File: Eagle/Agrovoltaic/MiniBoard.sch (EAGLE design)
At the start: 56 parts, among them J1 WAGO-03BE, J2 WAGO-03BE, J3 WAGO-03BE, K1 SRD-05VDC-SL-C, K3 SRD-05VDC-SL-C, Q1 BC338, Q2 BC338

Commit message: EDIT:Mengedit Board
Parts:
- removed CA3: 100n, rcl:CPOL-EUE3.5-8
- removed MC1: DEVKIT_V1_ESP32-WROOM-32, DEVKIT_V1_ESP32-WROOM-32:DEVKIT_V1_ESP32-WROOM-32
- added ANALOG, DIGITAL-IN, DIGITAL-OUT: (no value), con-wago-500:W237-102
- added CA4: 100n, rcl:CPOL-EUE3.5-8
- added U$1: CP8-ADJ, userlib:CP8-ADJ
- added U1: ESP32-DEVKIT-V1, ESP32-DEVKIT-V1:ESP32-DEVKIT-V1
- added UART2: 332-02, con-garry:332-02
- R12, R14: value 3K -> 2K
- R25, R26: value 3K -> 180
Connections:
- removed net IO16: MC1.IO16
- removed net IO17: MC1.IO17
- removed net IO4: MC1.IO4
- removed net N$10: IOESP.4
- removed net N$11: IOESP.5
- removed net N$12: IOESP.6
- removed net N$13: IOESP.7
- removed net N$14: IOESP.8
- removed net N$23: CA3.+, MC1.EN
- removed net N$44: MC1.SD2
- removed net N$45: MC1.SD3
- removed net N$46: MC1.CMD
- removed net N$5: IOESP.1
- removed net N$61: MC1.IO0
- removed net N$64: MC1.SD1
- removed net N$65: MC1.SD0
- removed net N$66: MC1.CLK
- removed net N$8: IOESP.2
- removed net N$9: IOESP.3
- removed net R3: MC1.IO12
- removed net R4: MC1.IO13
- removed net S3: MC1.IO25
- removed net S4: MC1.IO26
- new net AI2: ANALOG-2.KL, CA2.+, DZA3.A, DZA4.C, RA21.2
- new net D12: IOESP.3, U1.D12
- new net D13: IOESP.4, U1.D13
- new net D25: IOESP.5, U1.D25
- new net D26: IOESP.6, U1.D26
- new net D4: IOESP.1, U1.D4
- new net D5: IOESP.2, U1.D5
- new net N$25: CA4.+, U1.EN
- new net RX2: U1.RX2, UART2-2.S
- new net TX2: U1.TX2, UART2-1.S
- net 12V: now also J1.3, U$1.IN+; no longer J1.1
- net 3V3: now also U1.3V3; no longer MC1.3V3
- net 5V: now also U$1.OUT+, U1.VIN; no longer MC1.EXT_5V
- net A1: now also U1.D32; no longer MC1.IO32, RA21.1, RA22.2, RA23.2
- net A2: now also RA21.1, RA22.2, RA23.2, U1.D33; no longer MC1.IO33
- net AI1: now also ANALOG-1.KL; no longer CA2.+, DZA3.A, DZA4.C, RA21.2
- net CS: no longer MC1.IO5
- net GND: now also CA4.-, J1.1, U$1.IN-, U$1.OUT-, U1.GND; no longer CA3.-, J1.3, MC1.GND1, MC1.GND2, MC1.GND3
- net IN1: now also DIGITAL-IN-1.KL
- net IN2: now also DIGITAL-IN-2.KL
- net MISO: now also U1.D19; no longer MC1.IO19
- net MOSI: now also U1.D23; no longer MC1.IO23
- net OUT1: now also DIGITAL-OUT-1.KL
- net OUT2: now also DIGITAL-OUT-2.KL
- net R1: now also U1.D27; no longer MC1.IO27
- net R2: now also U1.D14; no longer MC1.IO14
- net RR1: now also U1.D15; no longer MC1.IO15
- net RR2: now also U1.D2; no longer MC1.IO2
- net RX0: now also U1.RX0; no longer MC1.RXD0
- net S1: now also U1.D34; no longer MC1.IO34
- net S2: now also U1.D35; no longer MC1.IO35
- net SCK: now also U1.D18; no longer MC1.IO18
- net SCL: now also U1.D22; no longer MC1.IO22
- net SDA: now also U1.D21; no longer MC1.IO21
- net TX0: now also U1.TX0; no longer MC1.TXD0
- net VN: now also IOESP.8, U1.VN; no longer MC1.SENSOR_VN
- net VP: now also IOESP.7, U1.VP; no longer MC1.SENSOR_VP
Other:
- moved on the sheet: D1, D13, D14, D4, I2C, J1, OK10, OK3, R1, R19, R20, R6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

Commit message: Still Edit
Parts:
- added RA1, RA2, RA3, RA4, RA5: 10K, rcl:R-EU_0207/10
- added S1, S2, S3: FSM103A, FSM103A:FSM103A
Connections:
- new net N$5: RA1.2, RA5.1, S1.COM
- new net N$8: RA1.1, RA2.2, S2.COM
- new net N$9: RA2.1, RA3.2, S3.COM
- net 3V3: now also RA5.2
- net CS: now also U1.D5
- net D4: now also RA4.2, S1.NO, S2.NO, S3.NO
- net D5: no longer U1.D5
- net GND: now also RA3.1, RA4.1

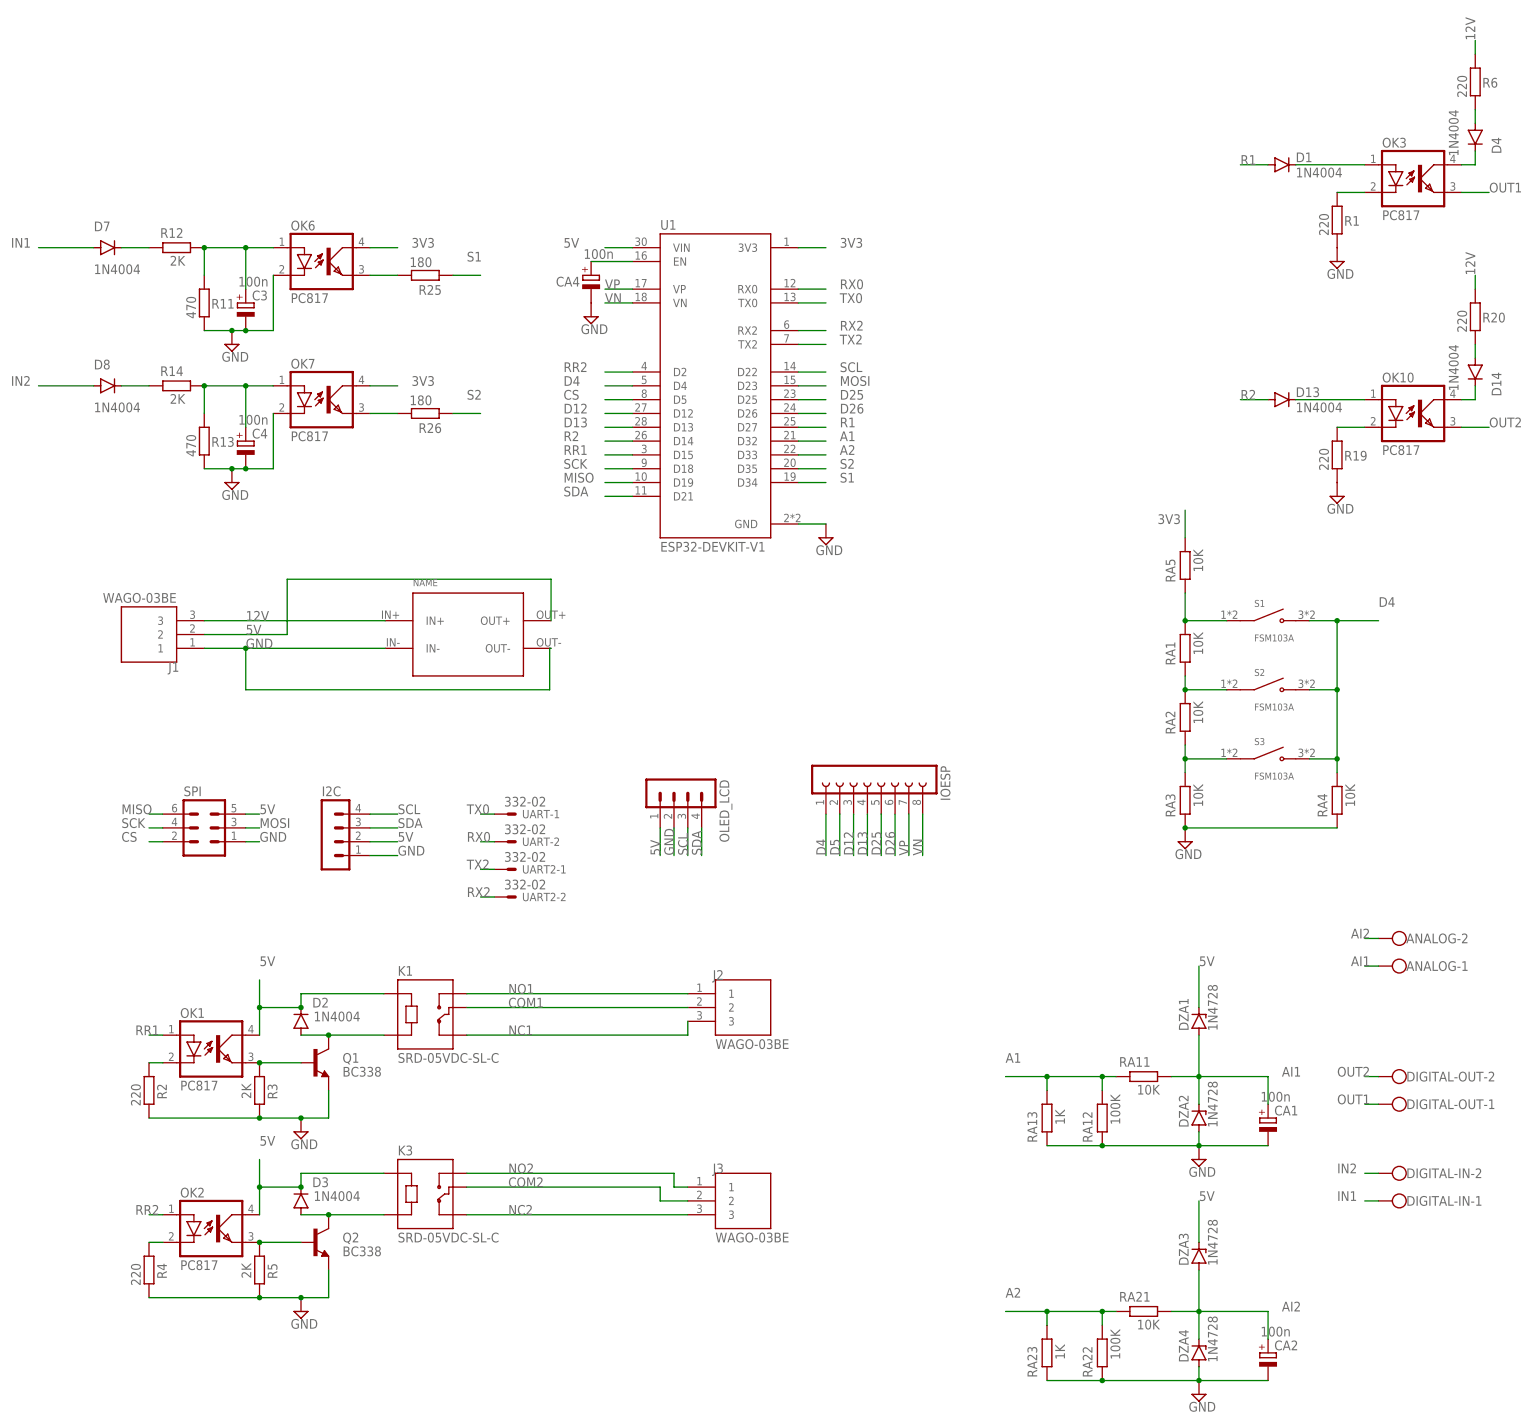
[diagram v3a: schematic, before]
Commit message: rapihin beberapa bagian, agar mudah diwire
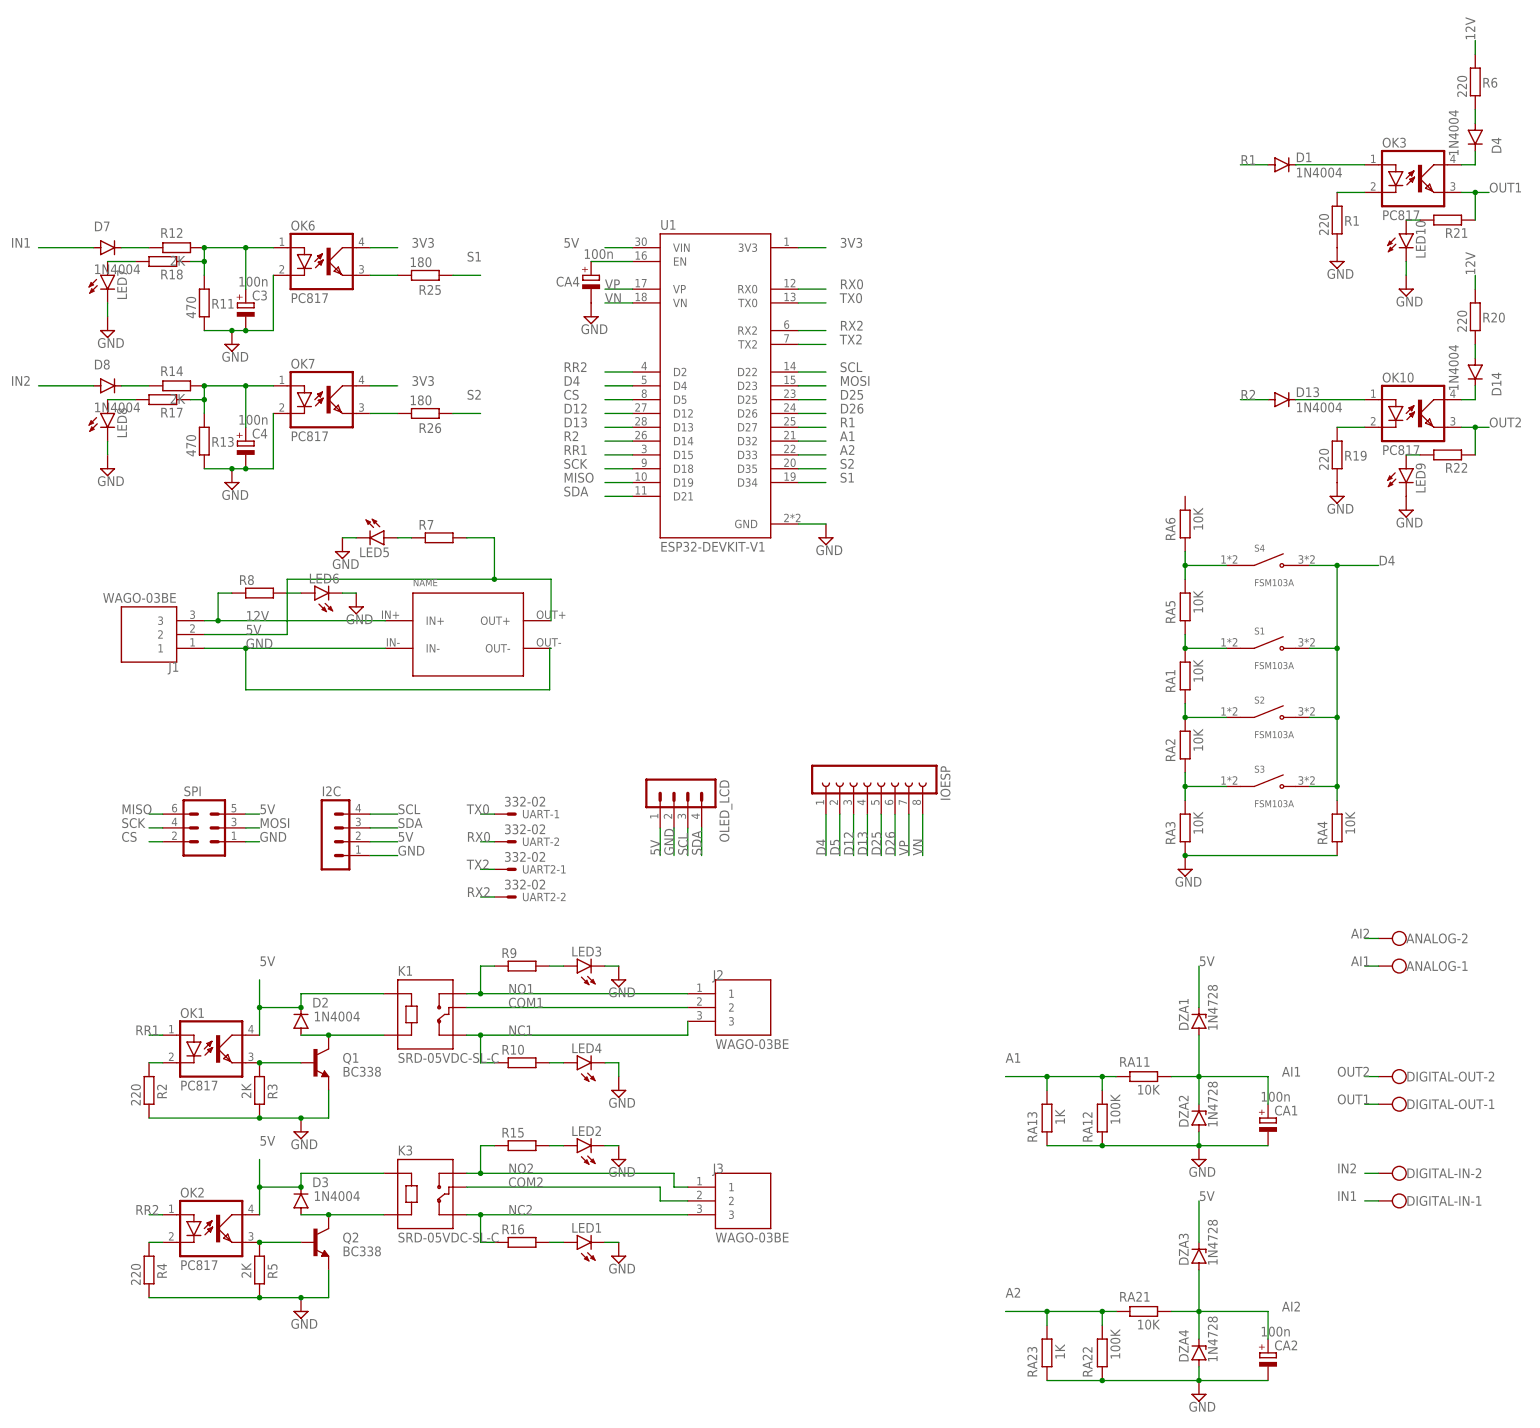
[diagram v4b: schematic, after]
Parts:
- added LED1, LED10, LED2, LED3, LED4, LED5, LED6, LED7, LED8, LED9: (no value), led_WS:LED3MM
- added R10, R15, R16, R17, R18, R21, R22, R7, R8, R9: (no value), rcl-ws:R-EU_0309/12
- added RA6: 10K, rcl-ws:R-EU_0309/12
- added S4: FSM103A, FSM103A:FSM103A
- C3, C4, CA1, CA2, CA4: device rcl:CPOL-EUE3.5-8 -> rcl-ws:CPOL-EUE5-6
- DZA1, DZA2, DZA3, DZA4: device diode:1N4728 -> diode-ws:1N4728
- R1, R11, R12, R13, R14, R19, R2, R20, R25, R26, R3, R4, R5, R6, RA1, RA11, RA12, RA13, RA2, RA21, RA22, RA23, RA3, RA4, RA5: device rcl:R-EU_0207/10 -> rcl-ws:R-EU_0309/12
- SPI: device con-lstb:MA03-2 -> con-lstb-ws:MA03-2
- UART, UART2: device con-garry:332-02 -> con-garry-ws:332-02
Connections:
- new net N$10: LED2.A, R15.2
- new net N$11: LED1.A, R16.2
- new net N$12: LED3.A, R9.2
- new net N$13: LED4.A, R10.2
- new net N$14: LED6.A, R8.2
- new net N$23: LED5.A, R7.1
- new net N$24: LED8.A, R17.2
- new net N$29: LED7.A, R18.2
- new net N$30: LED10.A, R21.2
- new net N$31: LED9.A, R22.2
- new net N$32: RA5.2, RA6.1, S4.COM
- net 12V: now also R8.1
- net 3V3: no longer RA5.2
- net 5V: now also R7.2
- net D4: now also S4.NO
- net GND: now also LED1.C, LED10.C, LED2.C, LED3.C, LED4.C, LED5.C, LED6.C, LED7.C, LED8.C, LED9.C
- net N$19: now also R18.1
- net N$21: now also R17.1
- net NC1: now also R10.1
- net NC2: now also R16.1
- net NO1: now also R9.1
- net NO2: now also R15.1
- net OUT1: now also R21.1
- net OUT2: now also R22.1
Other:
- moved on the sheet: RA1, RA2, RA3, RA4, RA5, S1, S2, S3

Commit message: MODIFY:Memisahkan Space Board
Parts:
- removed R20, R6: 220, rcl-ws:R-EU_0309/12
- renumbered LED1 to LNC2, LED10 to LO1, LED2 to LNO2, LED3 to LNO1, LED4 to LNC1, LED5 to L5, LED6 to L12, LED7 to LI1, LED8 to LI2, LED9 to LO2, R17 to RLI2, R18 to RLI1, R7 to RL5, R8 to RL12
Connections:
- removed net N$17: D4.A, R6.2
- removed net N$28: D14.A, R20.2
- net 12V: now also D14.A, D2.C, D3.C, D4.A, K1.A1, K3.A1, OK1.COL, OK2.COL; no longer R20.1, R6.1
- net 3V3: now also RA6.2
- net 5V: no longer D2.C, D3.C, K1.A1, K3.A1, OK1.COL, OK2.COL
- net D4: now also RA1.2; no longer RA4.2
- net GND: now also RA1.1, RA2.1; no longer RA3.1, RA4.1
- net N$5: now also RA4.2, S3.COM; no longer RA1.2, S1.COM
- net N$8: now also RA3.2, RA4.1; no longer RA1.1, RA2.2
- net N$9: now also RA2.2, RA3.1, S1.COM; no longer RA2.1, RA3.2, S3.COM
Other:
- moved on the sheet: RA1, RA2, RA3, RA4, S1, S3

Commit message: FINISHING
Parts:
- removed IOESP: (no value), con-lsta:FE08-1
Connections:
- removed net D5: IOESP.2
- net D12: no longer IOESP.3
- net D13: no longer IOESP.4
- net D25: no longer IOESP.5
- net D26: no longer IOESP.6
- net D4: no longer IOESP.1
- net VN: no longer IOESP.8
- net VP: no longer IOESP.7
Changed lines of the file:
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@@
 <part name="UART" library="con-garry-ws" deviceset="332-02" device="" package3d_urn="urn:adsk.eagle:package:6810/1"/>
 <part name="OLED_LCD" library="con-lstb" library_urn="urn:adsk.eagle:library:162" deviceset="MA04-1" device="" package3d_urn="urn:adsk.eagle:package:8337/1"/>
-<part name="IOESP" library="con-lsta" library_urn="urn:adsk.eagle:library:161" deviceset="FE08-1" device="" package3d_urn="urn:adsk.eagle:package:8194/1"/>
 <part name="OK10" library="optocoupler" library_urn="urn:adsk.eagle:library:320" deviceset="PC817" device="" package3d_urn="urn:adsk.eagle:package:21938/1"/>
 <part name="D13" library="diode" library_urn="urn:adsk.eagle:library:44429216" deviceset="1N4004" device="" package3d_urn="urn:adsk.eagle:package:44429257/2"/>
@@
 <attribute name="NAME" x="120.142" y="97.79" size="1.778" layer="95" rot="R270"/>
 </instance>
-<instance part="IOESP" gate="G$1" x="147.32" y="99.06" smashed="yes" rot="R270" grouprefs="IO_ESP32">
-<attribute name="VALUE" x="134.62" y="100.33" size="1.778" layer="96" rot="R270"/>
-<attribute name="NAME" x="160.782" y="100.33" size="1.778" layer="95" rot="R270"/>
-</instance>
 <instance part="OK10" gate="A" x="248.92" y="165.1" smashed="yes" grouprefs="DIGITAL_OUTPUT">
 <attribute name="NAME" x="241.935" y="170.815" size="1.778" layer="95"/>
@@
 </segment>
 <segment>
-<pinref part="IOESP" gate="G$1" pin="7"/>
 <wire x1="154.94" y1="91.44" x2="154.94" y2="83.82" width="0.1524" layer="91" grouprefs="IO_ESP32"/>
 <label x="154.94" y="83.82" size="1.778" layer="95" rot="R90"/>
@@
 </segment>
 <segment>
-<pinref part="IOESP" gate="G$1" pin="8"/>
 <wire x1="157.48" y1="91.44" x2="157.48" y2="83.82" width="0.1524" layer="91" grouprefs="IO_ESP32"/>
 <label x="157.48" y="83.82" size="1.778" layer="95" rot="R90"/>
@@
 </segment>
 <segment>
-<pinref part="IOESP" gate="G$1" pin="6"/>
 <wire x1="152.4" y1="91.44" x2="152.4" y2="83.82" width="0.1524" layer="91" grouprefs="IO_ESP32"/>
 <label x="152.4" y="83.82" size="1.778" layer="95" rot="R90"/>
@@
 </segment>
 <segment>
-<pinref part="IOESP" gate="G$1" pin="5"/>
 <wire x1="149.86" y1="91.44" x2="149.86" y2="83.82" width="0.1524" layer="91" grouprefs="IO_ESP32"/>
 <label x="149.86" y="83.82" size="1.778" layer="95" rot="R90"/>
@@
 </segment>
 <segment>
-<pinref part="IOESP" gate="G$1" pin="1"/>
 <wire x1="139.7" y1="91.44" x2="139.7" y2="83.82" width="0.1524" layer="91" grouprefs="IO_ESP32"/>
 <label x="139.7" y="83.82" size="1.778" layer="95" rot="R90"/>
@@
 <net name="D5" class="0">
 <segment>
-<pinref part="IOESP" gate="G$1" pin="2"/>
 <wire x1="142.24" y1="91.44" x2="142.24" y2="83.82" width="0.1524" layer="91" grouprefs="IO_ESP32"/>
 <label x="142.24" y="83.82" size="1.778" layer="95" rot="R90"/>
@@
 </segment>
 <segment>
-<pinref part="IOESP" gate="G$1" pin="3"/>
 <wire x1="144.78" y1="91.44" x2="144.78" y2="83.82" width="0.1524" layer="91" grouprefs="IO_ESP32"/>
 <label x="144.78" y="83.82" size="1.778" layer="95" rot="R90"/>
@@
 </segment>
 <segment>
-<pinref part="IOESP" gate="G$1" pin="4"/>
 <wire x1="147.32" y1="91.44" x2="147.32" y2="83.82" width="0.1524" layer="91" grouprefs="IO_ESP32"/>
 <label x="147.32" y="83.82" size="1.778" layer="95" rot="R90"/>

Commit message: REV:Revisi rangkaian 1
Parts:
- RA11, RA21: value 10K -> 100K
- RA12, RA22: value 100K -> 10K
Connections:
- removed net N$49: OK6.EMIT, R25.2
- removed net N$50: OK7.EMIT, R26.2
- net GND: now also R10.2, R15.2, R16.2, R21.2, R22.2, R25.1, R26.1, R9.2; no longer LNC1.C, LNC2.C, LNO1.C, LNO2.C, LO1.C, LO2.C
- net N$10: now also LNO2.C, R15.1; no longer LNO2.A, R15.2
- net N$11: now also LNC2.C, R16.1; no longer LNC2.A, R16.2
- net N$12: now also LNO1.C, R9.1; no longer LNO1.A, R9.2
- net N$13: now also LNC1.C, R10.1; no longer LNC1.A, R10.2
- net N$30: now also LO1.C, R21.1; no longer LO1.A, R21.2
- net N$31: now also LO2.C, R22.1; no longer LO2.A, R22.2
- net NC1: now also LNC1.A; no longer R10.1
- net NC2: now also LNC2.A; no longer R16.1
- net NO1: now also LNO1.A; no longer R9.1
- net NO2: now also LNO2.A; no longer R15.1
- net OUT1: now also LO1.A; no longer R21.1
- net OUT2: now also LO2.A; no longer R22.1
- net S1: now also OK6.EMIT, R25.2; no longer R25.1
- net S2: now also OK7.EMIT, R26.2; no longer R26.1
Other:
- moved on the sheet: LNC1, LNC2, LNO1, LNO2, LO1, LO2, R10, R15, R16, R21, R22, R25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

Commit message: Revisi lagiii
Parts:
- removed LNC1, LNC2: (no value), led_WS:LED3MM
- removed R10, R15, R16, R9: (no value), rcl-ws:R-EU_0309/12
- added A1: LM35DZ/NOPB, LM35DZ_NOPB:LM35DZ/NOPB
- added PAD1, PAD10, PAD100, PAD101, PAD102, PAD103, PAD104, PAD11, PAD12, PAD13, PAD14, PAD15, PAD16, PAD17, PAD18, PAD19, PAD2, PAD20, PAD21, PAD22, PAD23, PAD24, PAD25, PAD26, PAD27, PAD28, PAD29, PAD3, PAD30, PAD31, PAD32, PAD33, PAD34, PAD35, PAD36, PAD37, PAD38, PAD39, PAD4, PAD40, PAD41, PAD42, PAD43, PAD44, PAD45, PAD46, PAD47, PAD48, PAD49, PAD5, PAD50, PAD51, PAD52, PAD53, PAD54, PAD55, PAD56, PAD57, PAD58, PAD59, PAD6, PAD60, PAD61, PAD62, PAD63, PAD64, PAD65, PAD66, PAD67, PAD68, PAD69, PAD7, PAD70, PAD71, PAD72, PAD73, PAD74, PAD75, PAD76, PAD77, PAD78, PAD79, PAD8, PAD80, PAD81, PAD82, PAD83, PAD84, PAD85, PAD86, PAD87, PAD88, PAD89, PAD9, PAD90, PAD91, PAD92, PAD93, PAD94, PAD95, PAD96, PAD97, PAD98, PAD99: WIREPAD1,6/0,9, wirepad-ws:WIREPAD1,6/0,9
- added RLM35: (no value), rcl-ws:R-EU_0309/12
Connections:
- removed net N$11: LNC2.C, R16.1
- removed net N$13: LNC1.C, R10.1
- net 5V: now also A1.+VS
- net D25: now also A1.VOUT, RLM35.2
- net GND: now also A1.GND, R5.1, RLM35.1; no longer R10.2, R15.2, R16.2, R5.2, R9.2
- net N$10: now also R5.2; no longer R15.1
- net N$12: now also R3.1; no longer R9.1
- net N$3: now also LNO1.A; no longer R3.1
- net N$6: now also LNO2.A; no longer R5.1
- net NC1: no longer LNC1.A
- net NC2: no longer LNC2.A
- net NO1: no longer LNO1.A
- net NO2: no longer LNO2.A
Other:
- moved on the sheet: LNO1, LNO2, R3, R5
